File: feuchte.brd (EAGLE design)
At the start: 100 x 80 mm, 24 parts, among them CON1 CON_PCB_7.5MM_3-POLE, CON2 CON_PCB_7.5MM_3-POLE, IC1 IC_ULN2003AD, IC2 ESD_USB_IP4234CZ6, K1 RELAY_G5LA, K2 RELAY_G5LA, Q1 16MHz, U1 MCU_ATMEGA32U2-AU

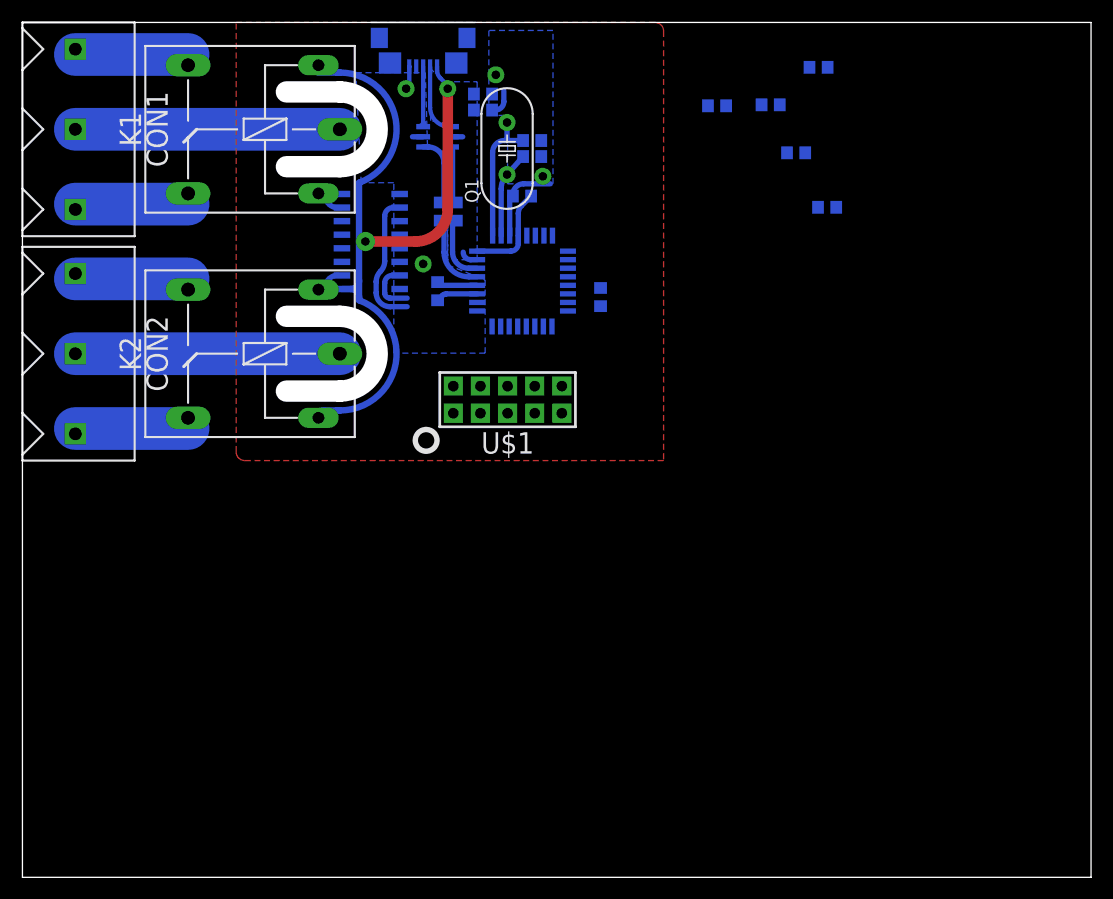
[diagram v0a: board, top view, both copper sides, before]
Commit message: 2 Kanäle + SHS-A5 im Schaltplan eingefügt
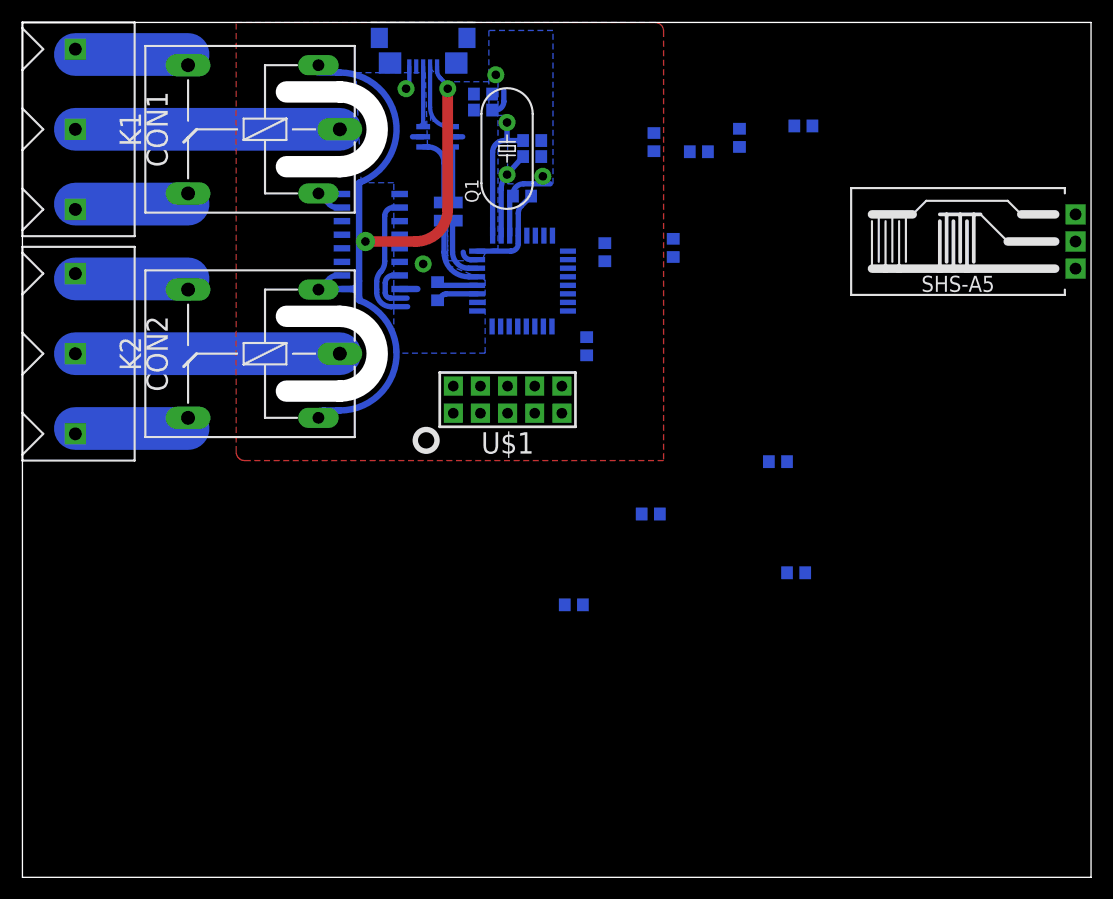
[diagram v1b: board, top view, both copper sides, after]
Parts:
- added C11, C12: 33n, Bauelemente:0603
- added R5, R6: 1k, Bauelemente:0603
- added R7: 4.7k, Bauelemente:0603
- added U$2: SENS_SHS-A5, Bauelemente:SENS_SHS-A5
- R1: value 1k -> 4.7k
- moved C9 55.3 mm to (51.6, 25.5)
- moved C10 34.3 mm to (72.4, 28.5)
- moved C7 6.81 mm to (59.1, 68.8), turned to 90 degrees
- moved C8 5.48 mm to (67.1, 69.2), turned to 90 degrees
- moved R4 4.78 mm to (52.8, 49.7)
- moved R1 3.64 mm to (73.1, 70.3), turned to 180 degrees
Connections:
- new net CAP2: R7.2
- new net N$22: C11.1, C12.1, U1.8
- new net N$23: C12.2, U$2.3, U1.9
- new net N$24: U1.6
- new net N$25: C11.2, U$2.2, U1.10
- new net N$26: C9.1, R6.2
- new net N$27: C10.1, R6.1, U1.11
- new net N$28: C10.2, C9.2, R7.1, U1.12
- net GND: now also U$2.1
- net N$10: now also C8.1, R5.2; no longer C10.1, C9.2
- net N$8: now also R5.1; no longer C8.1, C9.1, U1.7
- net N$9: now also U1.7; no longer C10.2, U1.8
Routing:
- net GND: track 17.0 -> 18.6 mm

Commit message: ISP Stecker gelayouted, dabei die Relaisversorgung angefasst
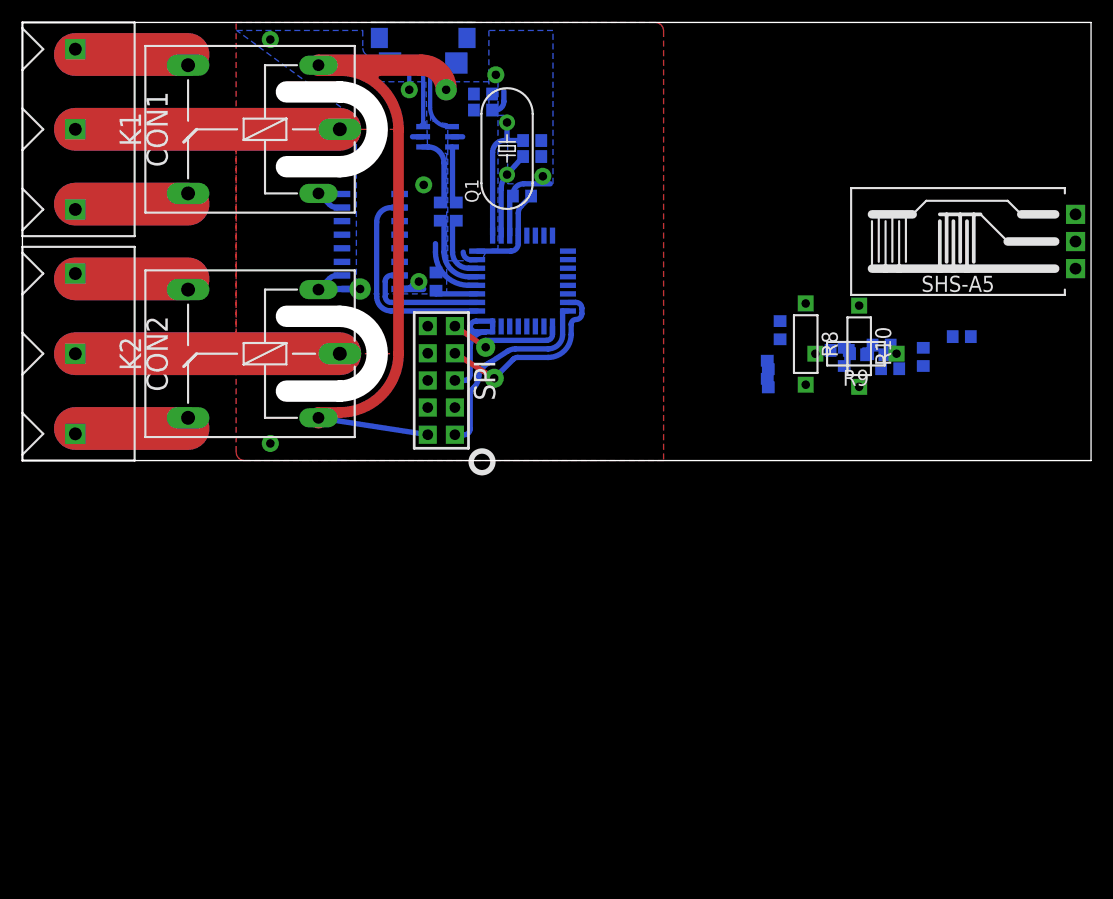
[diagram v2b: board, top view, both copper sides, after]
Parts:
- removed U$1: CON_SPI_AVR10, Bauelemente:CON_ISP_AVR10
- removed U1: MCU_ATMEGA32U2-AU, Bauelemente:TQFP32-0.8
- added IC3: IC_ULN2003AD, Bauelemente:SOIC16
- added R10, R8, R9: (no value), Bauelemente:R_THT_7.5MM
- added SPI: CON_SPI_AVR10, Bauelemente:CON_ISP_AVR10
- IC1: value IC_ULN2003AD -> IC_ATMEGA32U2-AU; device Bauelemente:SOIC16 -> Bauelemente:IC_ATMEGA32U2-AU
- IC2: device Bauelemente:USB_ESD_IP4234CZ6 -> Bauelemente:ESD_USB_IP4234CZ6
- moved C9 36.6 mm to (79.8, 48.9)
- moved R4 31.5 mm to (84.3, 48.7)
- moved R5 30.1 mm to (87.9, 50.6)
- moved R6 26.8 mm to (80.4, 49.8)
- moved C7 23.8 mm to (69.7, 47.5)
- moved C8 22.7 mm to (69.8, 46.7)
- moved R1 21.3 mm to (76.5, 49.3)
- moved C10 21.0 mm to (81.2, 47.6)
- moved C11 19.0 mm to (76.9, 48.7)
- moved C12 18.0 mm to (70.9, 51.2)
- moved IC1 14.7 mm to (46.8, 55.8)
- moved R7 12.6 mm to (78.3, 49.0)
- moved C5 0.91 mm to (38.7, 55.8)
- renumbered USB1 to USB
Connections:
- net USBCON_ renamed USBCON_P
- net USBR_ renamed USBR_N
- removed net N$22: C11.1, C12.1, U1.8
- removed net USBC_: R3.2, U1.30
- new net N$29: IC1.7, R10.2, R8.1, R9.1
- new net N$30: IC1.14, R8.2
- new net USBC_N: IC1.30, R3.2
- net +3V3: now also IC1.27; no longer U1.27
- net +5V: now also IC1.31, IC1.32, IC1.4, IC3.9, R9.2, SPI.2; no longer IC1.9, U$1.2, U1.31, U1.32, U1.4
- net GND: now also IC1.28, IC3.1, IC3.3, IC3.4, IC3.5, IC3.6, IC3.8, R10.1, SPI.10, SPI.4, SPI.6, SPI.8; no longer IC1.1, IC1.4, IC1.5, IC1.6, IC1.8, U$1.10, U$1.4, U$1.6, U$1.8, U1.28, U1.3
- net N$1: now also IC1.1; no longer U1.1
- net N$11: now also IC1.26, IC3.7; no longer IC1.7, U1.23
- net N$12: now also IC1.25, IC3.2; no longer IC1.2, U1.21
- net N$13: now also IC3.10; no longer IC1.10
- net N$14: now also IC3.15; no longer IC1.15
- net N$2: now also IC1.2; no longer U1.2
- net N$20: now also IC1.13; no longer U1.13
- net N$23: no longer U1.9
- net N$24: now also C11.1, C12.1; no longer U1.6
- net N$25: no longer U1.10
- net N$27: no longer U1.11
- net N$28: no longer U1.12
- net N$3: now also IC1.15, SPI.7; no longer U$1.7, U1.15
- net N$4: now also IC1.16, SPI.1; no longer U$1.1, U1.16
- net N$5: now also IC1.17, SPI.9; no longer U$1.9, U1.17
- net N$6: now also IC1.24, SPI.5; no longer U$1.5, U1.24
- net N$9: no longer U1.7
- net USBC_P: now also IC1.29; no longer U1.29
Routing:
- net N$35: track 0.00 -> 24.8 mm
- net N$31: track 0.00 -> 24.8 mm
- net N$4: track 0.00 -> 18.9 mm
- net N$3: track 0.00 -> 17.6 mm, vias 0 -> 1
- net N$6: track 0.00 -> 13.8 mm
- net N$36: track 0.00 -> 12.1 mm
- net N$34: track 0.00 -> 12.1 mm
- net N$33: track 0.00 -> 12.1 mm
- net N$32: track 0.00 -> 12.1 mm
- net N$5: track 0.00 -> 11.4 mm, vias 0 -> 1
- net N$12: track 12.5 -> 19.6 mm
- net N$11: track 4.82 -> 11.8 mm
- net USBC_N: track 0.00 -> 6.22 mm
- net USBC_: track 6.22 -> 0.00 mm
- net GND: track 18.6 -> 22.9 mm, vias 4 -> 7
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- added copper zone on layer 1, net +5V
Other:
- board size 100 x 80 mm -> 100 x 41 mm

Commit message: Layout geschätzt bei 80%
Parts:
- removed C11, C12: 33n, Bauelemente:0603
- removed R5, R6: 1k, Bauelemente:0603
- C8, C9: value 100n -> 33n
- R8: device Bauelemente:R_THT_7.5MM -> Bauelemente:R_THT_10MM
- moved R10 40.8 mm to (46.9, 75.7), turned to 0 degrees
- moved R4 36.0 mm to (48.4, 47.5), turned to 180 degrees
- moved R9 34.1 mm to (49.5, 67.8), turned to 270 degrees
- moved R1 27.0 mm to (53.4, 63.3), turned to 90 degrees
- moved C10 25.6 mm to (55.8, 51.1)
- moved C9 24.5 mm to (56.8, 57.5), turned to 270 degrees
- moved C7 23.8 mm to (51.9, 63.3), turned to 270 degrees
- moved R7 22.5 mm to (55.8, 49.6), turned to 180 degrees
- moved R8 21.5 mm to (52.6, 55.9), turned to 270 degrees
- moved C8 18.1 mm to (55.3, 57.5), turned to 270 degrees
- moved U$2 8.50 mm to (98.6, 51.0)
- moved IC2 1.30 mm to (38.9, 68.0)
- moved R2 0.40 mm to (39.1, 61.9)
- moved R3 0.40 mm to (40.6, 61.9)
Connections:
- removed net N$23: C12.2, U$2.3
- removed net N$26: C9.1, R6.2
- removed net N$28: C10.2, C9.2, R7.1
- new net N$22: C9.2, IC1.8, U$2.3
- net N$10: now also C10.1, IC1.11; no longer C8.1, R5.2
- net N$24: now also C8.1, C9.1, IC1.9; no longer C11.1, C12.1
- net N$25: now also C8.2, IC1.10; no longer C11.2
- net N$27: now also C10.2, IC1.12, R7.1; no longer C10.1, R6.1
- net N$8: now also IC1.5; no longer R5.1
- net N$9: now also IC1.6; no longer C8.2
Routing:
- net N$22: track 0.00 -> 55.0 mm
- net N$25: track 0.00 -> 50.1 mm
- net N$29: track 0.00 -> 21.0 mm
- net N$20: track 0.00 -> 12.7 mm
- net N$10: track 0.00 -> 8.41 mm
- net N$27: track 0.00 -> 8.08 mm
- net N$9: track 0.00 -> 7.03 mm
- net N$8: track 0.00 -> 6.72 mm
- net N$24: track 0.00 -> 6.15 mm
- net N$6: track 13.8 -> 7.91 mm
- net N$30: track 0.00 -> 5.18 mm
- net +5V: track 81.3 -> 85.3 mm
- net USBCON_P: track 6.76 -> 8.06 mm
- net USBCON_N: track 6.62 -> 7.92 mm
- net USBR_P: track 6.62 -> 5.72 mm
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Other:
- outline, holes or cut-outs redrawn

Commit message: weiter gelayout
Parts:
- moved R4 0.25 mm to (48.6, 47.5)
- moved R10 0.10 mm to (46.9, 75.8)
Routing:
- net N$7: track 24.8 -> 49.5 mm
- net N$35: track 24.8 -> 0.00 mm
- net N$31: track 24.8 -> 0.00 mm
- net N$18: track 24.8 -> 49.5 mm
- net N$36: track 12.1 -> 0.00 mm
- net N$34: track 12.1 -> 0.00 mm
- net N$33: track 12.1 -> 0.00 mm
- net N$32: track 12.1 -> 0.00 mm
- net N$19: track 12.1 -> 24.1 mm
- net N$17: track 12.1 -> 24.1 mm
- net N$16: track 12.1 -> 24.1 mm
- net N$15: track 12.1 -> 24.1 mm
- net GND: track 22.4 -> 28.9 mm, vias 6 -> 4
- net N$29: track 21.0 -> 21.7 mm

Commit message: neues dru
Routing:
- net N$22: track 55.0 -> 56.0 mm
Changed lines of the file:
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@@
 </class>
 </classes>
-<designrules name="pcb-devboards_35µmCU_200µm_Strukturen_Abstaende *">
-<description language="de">
-pcb-devboards.de Standard DRU-File.
-Bohrungen NDK+DK: 0,3 - 6,3mm (in 0,1mm Schritten)
-Ab 6,3mm werden die Bohrungen gefräst, daher die Bohrung mit Umriss-Layer zeichnen.
-Leiterplatten Dicke: 0,5 - 1,6mm
-Kupferstärke: nur 35µm
-Struktur/Abstand/Restring umlaufend: 200µm
-</description>
-<description language="en">
-&lt;b&gt;EAGLE Design Rules&lt;/b&gt;
+<designrules name="platinensammler_03 *">
+<description language="de">&lt;b&gt; DRC-File für Sammelnutzen. &lt;/b&gt;&lt;br&gt;&lt;br&gt;
+Die in diesen Designregeln festgelegten Maße, Abstände und Durchmesser stellen die Mindestanforderungen für eine Teilnahme am Sammelnutzen dar und lauten wie folgt:&lt;br&gt;&lt;br&gt;
+&lt;table border=1&gt;
+&lt;tr&gt;
+&lt;th&gt;Bezeichnung&lt;/th&gt;
+&lt;th&gt;Maß&lt;/th&gt;
+&lt;/tr&gt;
+&lt;tr&gt;
+&lt;td&gt;min. Leiterbahnenbreite &lt;/td&gt;
+&lt;td&gt;0,15mm&lt;/td&gt;
+&lt;/tr&gt;
+&lt;tr&gt;
+&lt;td&gt;min. Leiterbahnenabstand &lt;/td&gt;
+&lt;td&gt;0,15mm&lt;/td&gt;
+&lt;/tr&gt;
+&lt;tr&gt;
+&lt;td&gt;min. Abstand Kupfer zu Kontur   &lt;/td&gt;
+&lt;td&gt;0,2mm&lt;/td&gt;
+&lt;/tr&gt;
+&lt;tr&gt;
+&lt;td&gt;&lt;/td&gt;
+&lt;td&gt;&lt;/td&gt;
+&lt;/tr&gt;
+&lt;tr&gt;
+&lt;td&gt;min. Bohrdurchmesser&lt;/td&gt;
+&lt;td&gt;0,3mm&lt;/td&gt;
+&lt;/tr&gt;
+&lt;/table&gt;
+&lt;br&gt;&lt;br&gt;
+Alle Durchkontaktierungen unter 0,8mm gelten als Via und werden abgedeckt.&lt;br&gt; (kann man über &quot;Masks/Limit&quot; verändern)&lt;br&gt;&lt;br&gt;
+Thermals für Vias sind ausgeschaltet (kann man über &quot;Supply/generate thermals for vias&quot; einschalten)&lt;br&gt;&lt;br&gt;
+Natürlich können Sie alle Einstellungen &quot;nach oben&quot; korregieren, wenn Sie dies für Ihr Layout benötigen.&lt;br&gt;&lt;br&gt;
+Sollten Sie Fragen zu den Designregeln haben, können Sie mich über &lt;b&gt;platinensammler@gmail.com&lt;/b&gt; erreichen.&lt;br&gt;&lt;br&gt;
+Jakob Kleinen</description>
+<description language="en">&lt;b&gt;EAGLE Design Rules&lt;/b&gt;
 &lt;p&gt;
 The default Design Rules have been set to cover
@@
 <param name="mtCopper" value="0.035mm 0.035mm 0.035mm 0.035mm 0.035mm 0.035mm 0.035mm 0.035mm 0.035mm 0.035mm 0.035mm 0.035mm 0.035mm 0.035mm 0.035mm 0.035mm"/>
 <param name="mtIsolate" value="1.5mm 0.15mm 0.2mm 0.15mm 0.2mm 0.15mm 0.2mm 0.15mm 0.2mm 0.15mm 0.2mm 0.15mm 0.2mm 0.15mm 0.2mm"/>
-<param name="mdWireWire" value="0.25mm"/>
-<param name="mdWirePad" value="0.25mm"/>
-<param name="mdWireVia" value="0.25mm"/>
-<param name="mdPadPad" value="0.25mm"/>
-<param name="mdPadVia" value="0.25mm"/>
-<param name="mdViaVia" value="0.25mm"/>
-<param name="mdSmdPad" value="0.25mm"/>
-<param name="mdSmdVia" value="0.25mm"/>
-<param name="mdSmdSmd" value="0.25mm"/>
+<param name="mdWireWire" value="0.15mm"/>
+<param name="mdWirePad" value="0.15mm"/>
+<param name="mdWireVia" value="0.15mm"/>
+<param name="mdPadPad" value="0.15mm"/>
+<param name="mdPadVia" value="0.15mm"/>
+<param name="mdViaVia" value="0.15mm"/>
+<param name="mdSmdPad" value="0mil"/>
+<param name="mdSmdVia" value="0mil"/>
+<param name="mdSmdSmd" value="0mil"/>
 <param name="mdViaViaSameLayer" value="8mil"/>
 <param name="mnLayersViaInSmd" value="2"/>
-<param name="mdCopperDimension" value="0.4746mm"/>
-<param name="mdDrill" value="1mm"/>
+<param name="mdCopperDimension" value="0.2mm"/>
+<param name="mdDrill" value="0.2mm"/>
 <param name="mdSmdStop" value="0mil"/>
-<param name="msWidth" value="0.4mm"/>
-<param name="msDrill" value="0.8mm"/>
-<param name="msMicroVia" value="0.4mm"/>
+<param name="msWidth" value="0.15mm"/>
+<param name="msDrill" value="0.3mm"/>
+<param name="msMicroVia" value="0.3mm"/>
 <param name="msBlindViaRatio" value="0.5"/>
-<param name="rvPadTop" value="0.4"/>
-<param name="rvPadInner" value="0.4"/>
-<param name="rvPadBottom" value="0.4"/>
+<param name="rvPadTop" value="0.25"/>
+<param name="rvPadInner" value="0.25"/>
+<param name="rvPadBottom" value="0.25"/>
 <param name="rvViaOuter" value="0.5"/>
 <param name="rvViaInner" value="0.5"/>
@@
 <param name="rvMicroViaInner" value="0.25"/>
 <param name="rlMinPadTop" value="0.35mm"/>
-<param name="rlMaxPadTop" value="0.35mm"/>
+<param name="rlMaxPadTop" value="20mil"/>
 <param name="rlMinPadInner" value="0.35mm"/>
-<param name="rlMaxPadInner" value="0.35mm"/>
+<param name="rlMaxPadInner" value="20mil"/>
 <param name="rlMinPadBottom" value="0.35mm"/>
-<param name="rlMaxPadBottom" value="0.35mm"/>
-<param name="rlMinViaOuter" value="0.4mm"/>
-<param name="rlMaxViaOuter" value="0.5mm"/>
-<param name="rlMinViaInner" value="0.4mm"/>
-<param name="rlMaxViaInner" value="0.5mm"/>
-<param name="rlMinMicroViaOuter" value="0.4mm"/>
-<param name="rlMaxMicroViaOuter" value="0.5mm"/>
-<param name="rlMinMicroViaInner" value="0.4mm"/>
-<param name="rlMaxMicroViaInner" value="0.5mm"/>
+<param name="rlMaxPadBottom" value="20mil"/>
+<param name="rlMinViaOuter" value="0.2mm"/>
+<param name="rlMaxViaOuter" value="20mil"/>
+<param name="rlMinViaInner" value="0.2mm"/>
+<param name="rlMaxViaInner" value="20mil"/>
+<param name="rlMinMicroViaOuter" value="0.2mm"/>
+<param name="rlMaxMicroViaOuter" value="20mil"/>
+<param name="rlMinMicroViaInner" value="0.2mm"/>
+<param name="rlMaxMicroViaInner" value="20mil"/>
 <param name="psTop" value="1"/>
 <param name="psBottom" value="1"/>
@@
 <param name="mvStopFrame" value="1"/>
 <param name="mvCreamFrame" value="0"/>
-<param name="mlMinStopFrame" value="0.15mm"/>
-<param name="mlMaxStopFrame" value="0.15mm"/>
-<param name="mlMinCreamFrame" value="1.5mil"/>
-<param name="mlMaxCreamFrame" value="1.5mil"/>
-<param name="mlViaStopLimit" value="0mil"/>
+<param name="mlMinStopFrame" value="2mil"/>
+<param name="mlMaxStopFrame" value="4mil"/>
+<param name="mlMinCreamFrame" value="0mil"/>
+<param name="mlMaxCreamFrame" value="0mil"/>
+<param name="mlViaStopLimit" value="0.8mm"/>
 <param name="srRoundness" value="0.5"/>
 <param name="srMinRoundness" value="0mil"/>
-<param name="srMaxRoundness" value="0.3mm"/>
-<param name="slThermalIsolate" value="0.3mm"/>
+<param name="srMaxRoundness" value="0.5mm"/>
+<param name="slThermalIsolate" value="0.15mm"/>
 <param name="slThermalsForVias" value="0"/>
-<param name="dpMaxLengthDifference" value="0.1mm"/>
+<param name="dpMaxLengthDifference" value="10mm"/>
 <param name="dpGapFactor" value="2.5"/>
 <param name="checkGrid" value="0"/>
@@
 <wire x1="51.05" y1="57.8" x2="52.40294375" y2="57.8" width="0.5" layer="16"/>
 <wire x1="52.40294375" y1="57.8" x2="55.3" y2="56.6" width="0.5" layer="16" curve="-45"/>
-<wire x1="98.6" y1="51" x2="95.384315625" y2="54.215684375" width="0.5" layer="16"/>
-<wire x1="95.384315625" y1="54.215684375" x2="94.818628125" y2="54.45" width="0.5" layer="16" curve="45.000224"/>
-<wire x1="94.818628125" y1="54.45" x2="58.556853125" y2="54.45" width="0.5" layer="16"/>
-<wire x1="58.556853125" y1="54.45" x2="55.728428125" y2="55.621571875" width="0.5" layer="16" curve="-44.999968"/>
-<wire x1="55.728428125" y1="55.621571875" x2="55.3" y2="56.05" width="0.5" layer="16"/>
-<wire x1="55.3" y1="56.05" x2="55.3" y2="56.6" width="0.5" layer="16"/>
+<wire x1="98.6" y1="51" x2="64.642134375" y2="51" width="0.5" layer="16"/>
+<wire x1="64.642134375" y1="51" x2="57.57106875" y2="53.92893125" width="0.5" layer="16" curve="-44.999987"/>
+<wire x1="57.57106875" y1="53.92893125" x2="55.3" y2="56.2" width="0.5" layer="16"/>
+<wire x1="55.3" y1="56.2" x2="55.3" y2="56.6" width="0.5" layer="16"/>
 </signal>
 <signal name="CAP2">
@@
 <contactref element="IC1" pad="8"/>
 <contactref element="U$2" pad="3"/>
-<wire x1="98.6" y1="53.54" x2="97.18289375" y2="54.95710625" width="0.5" layer="16"/>
-<wire x1="97.18289375" y1="54.95710625" x2="96.4757875" y2="55.25" width="0.5" layer="16" curve="45"/>
 <contactref element="C9" pad="2"/>
 <wire x1="49.6" y1="60.05" x2="49.6" y2="59.55" width="0.5" layer="16"/>
@@
 <wire x1="57.95" y1="57.853503125" x2="57.6255125" y2="57.2101625" width="0.5" layer="16" curve="-53.530773"/>
 <wire x1="57.6255125" y1="57.2101625" x2="56.8" y2="56.6" width="0.5" layer="16"/>
-<wire x1="96.4757875" y1="55.25" x2="58.731371875" y2="55.25" width="0.5" layer="16"/>
-<wire x1="58.731371875" y1="55.25" x2="56.8" y2="56.05" width="0.5" layer="16" curve="-45"/>
-<wire x1="56.8" y1="56.05" x2="56.8" y2="56.6" width="0.5" layer="16"/>
+<wire x1="98.6" y1="53.54" x2="97.021090625" y2="51.961090625" width="0.5" layer="16"/>
+<wire x1="97.021090625" y1="51.961090625" x2="96.63218125" y2="51.8" width="0.5" layer="16" curve="-45"/>
+<wire x1="96.63218125" y1="51.8" x2="65.010765625" y2="51.8" width="0.5" layer="16"/>
+<wire x1="65.010765625" y1="51.8" x2="58.50538125" y2="54.49461875" width="0.5" layer="16" curve="-45.000014"/>
+<wire x1="58.50538125" y1="54.49461875" x2="56.8" y2="56.2" width="0.5" layer="16"/>
+<wire x1="56.8" y1="56.2" x2="56.8" y2="56.6" width="0.5" layer="16"/>
 </signal>
 </signals>

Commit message: Layout V1 fertig
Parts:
- C1: value 10µ -> 10µF
- C6: value 100n -> 100nF
- moved U$2 0.40 mm to (98.2, 51.0)
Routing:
- net GND: track 28.9 -> 50.4 mm, vias 4 -> 30
- net CAP: track 0.00 -> 18.1 mm, vias 0 -> 13
- net CAP2: track 0.00 -> 13.7 mm, vias 0 -> 12
- net N$27: track 8.08 -> 8.83 mm
- added copper zone on layer 1, net CAP
- added copper zone on layer 16, net CAP
- added copper zone on layer 1, net CAP2
- added copper zone on layer 16, net CAP2
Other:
- outline, holes or cut-outs redrawn
- board text added: "Gießanlage Stefan Hellermann 08.07.2014"
